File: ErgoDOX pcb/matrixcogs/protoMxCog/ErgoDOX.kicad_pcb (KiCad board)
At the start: 2 copper layers, 182.8 x 158.9 mm, 77 parts, among them J1 USB, J2 3.5mm, J3 JMP, J4 JMP, SW0:10 SW0:3, SW0:11 SW0:2, SW0:12 SW0:1, SW0:7 SW0:6, SW0:8 SW0:5, SW0:9 SW0:4, SW1:10 SW1:3, SW1:11 SW1:2, SW1:12 SW1:1, SW1:13 SW1:0, SW1:9 SW1:4, SW2:10 SW2:3, SW2:11 SW2:2, SW2:12 SW2:1, SW2:13 SW2:0, SW2:7 SW2:6, SW2:8 SW2:5, SW2:9 SW2:4, SW3:10 SW3:3, SW3:11 SW3:2, SW3:12 SW3:1, SW3:13 SW3:0, SW3:8 SW3:5, SW3:9 SW3:4, SW4:10 SW4:3, SW4:11 SW4:2, SW4:12 SW4:1, SW4:13 SW4:0, SW4:7 SW4:6, SW4:8 SW4:5, SW4:9 SW4:4, SW5:10 SW5:3, SW5:11 SW5:2, SW5:12 SW5:1, SW5:13 SW5:0, SW5:7 SW5:6, SW5:8 SW5:5, SW5:9 SW5:4, U1 TEENSY2.0, U2 MCP23018

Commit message: removing top part of PCB on switch matrix board
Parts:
- removed J2: 3.5mm, 4pin35mmAudio
- removed J3, J4: JMP, 100PITCH1X3
- removed JP1, JP2: JUMPER, GAP
- removed LED_C1: LEDc, MX_LED
- removed RA1: LEDa, RESISTOR
- removed RB1: LEDb, RESISTOR
- removed RC1: LEDc, RESISTOR
- removed STAR_1: STAR_FRONT, ErgoDOX pcb:STAR
- removed STAR_2: STAR_BACK, ErgoDOX pcb:STAR
- removed STITCHING_VIA (x11): ~, lib_footprints:STITCHING_VIA
- removed SW_RST1: SWITCH_PUSH, Buttons_Switches_SMD:SW_SPST_B3U-1000P
- removed U1: TEENSY2.0, ErgoDOX pcb:TEENSY_2.0_WITH_RESET
- removed U2: MCP23018, DIP28_300
- D1:7, D1:8: footprint DIODE -> ergodox:DIODE
- H99: footprint ErgoDOXmech -> ergodox:ErgoDOXmech
- J1: value USB -> Conn_01x18; footprint USBMINImod -> ergodox:ErgoCogs_side_con
- LED_A1, LED_B1: footprint MX_LED -> LED_SMD:LED_0805_2012Metric_Pad1.15x1.40mm_HandSolder
- R1, R2: value 2.2kΩ -> 470; footprint RESISTOR -> Resistor_SMD:R_0603_1608Metric_Pad0.98x0.95mm_HandSolder
- S1, S2: footprint STAB_PCB940 -> ergodox:STAB_PCB940
- SW0:10, SW0:11, SW0:12, SW0:7, SW0:8, SW0:9, SW1:10, SW1:11, SW1:12, SW1:13, SW1:9, SW2:10, SW2:11, SW2:12, SW2:7, SW2:8, SW2:9, SW3:10, SW3:11, SW3:12, SW3:8, SW3:9, SW4:10, SW4:11, SW4:12, SW4:7, SW4:8, SW4:9, SW5:10, SW5:11, SW5:12, SW5:7, SW5:8, SW5:9: footprint ErgoDOX pcb:MX_FLIP_DIODE -> ergodox:MX_FLIP_DIODE
- SW2:13, SW3:13, SW4:13, SW5:13: footprint ErgoDOX pcb:MX_FLIP_XX -> ergodox:MX_FLIP_DIODE
- SX0:10, SX0:11, SX1:7, SX1:8: footprint MX_FLIP -> ergodox:MX_FLIP_DIODE
- moved J1 86.5 mm to (65.0, 77.3), turned to 0 degrees
- moved LED_B1 34.2 mm to (78.7, 55.3), turned to 0 degrees
- moved R1 26.6 mm to (83.3, 55.1), turned to 0 degrees
- moved R2 19.9 mm to (87.6, 55.1), turned to 0 degrees
- moved LED_A1 9.88 mm to (73.9, 55.3)
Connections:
- J1 pad 1: Net-(J1-Pad1) -> (no net)
- J1 pad 2: Net-(J1-Pad2) -> /ROW0
- J1 pad 3: Net-(J1-Pad3) -> /ROW1
- J1 pad 4: Net-(J1-Pad4) -> /ROW2
- J1 pad 5: Net-(J1-Pad5) -> /ROW3
- J1 pad 6: GND -> /ROW4
- R1 pad 1: VCC -> /LED_B
- R1 pad 2: /SDAM -> Net-(LED_A1-Pad1)
- R2 pad 1: VCC -> /LED_A
- R2 pad 2: /SCLM -> Net-(LED_B1-Pad1)
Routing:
- net VCC: track 204.8 -> 0.57 mm, vias 2 -> 1
- net /ROW0: track 404.2 -> 274.5 mm
- net /SDAM: track 128.3 -> 0.00 mm
- net /SCLM: track 119.7 -> 0.00 mm
- net /ROW1: track 318.2 -> 210.8 mm
- net Net-(J1-Pad1): track 102.6 -> 0.00 mm
- net /ROW2: track 295.3 -> 206.6 mm
- net Net-(LED_B1-Pad1): track 119.1 -> 35.7 mm
- net /ROW3: track 238.7 -> 168.8 mm
- net Net-(LED_A1-Pad1): track 87.6 -> 22.1 mm
- net Net-(J1-Pad5): track 62.3 -> 0.00 mm
- net Net-(LED_C1-Pad1): track 127.4 -> 65.8 mm
- net /COL5: track 225.8 -> 172.7 mm
- net /ROW4: track 257.4 -> 206.2 mm
- net /COL6: track 259.5 -> 208.6 mm
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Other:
- board size 182.8 x 158.9 mm -> 182.8 x 140.1 mm
- board text removed: "5V"
- board text removed: "D+"
- board text removed: "D-"
- board text removed: "Design by Dominic Beauchamp, based on the Key64 by Nestor A. Diaz"
- board text removed: "Drawn in KiCAD by Fredrik Atmer, Bathroom Epiphanies"
- board text removed: "ErgoDox"
- board text removed: "GND"
- board text removed: "ID"
- board text removed: "Revision 01-05-2017 ProfetKeyboards"

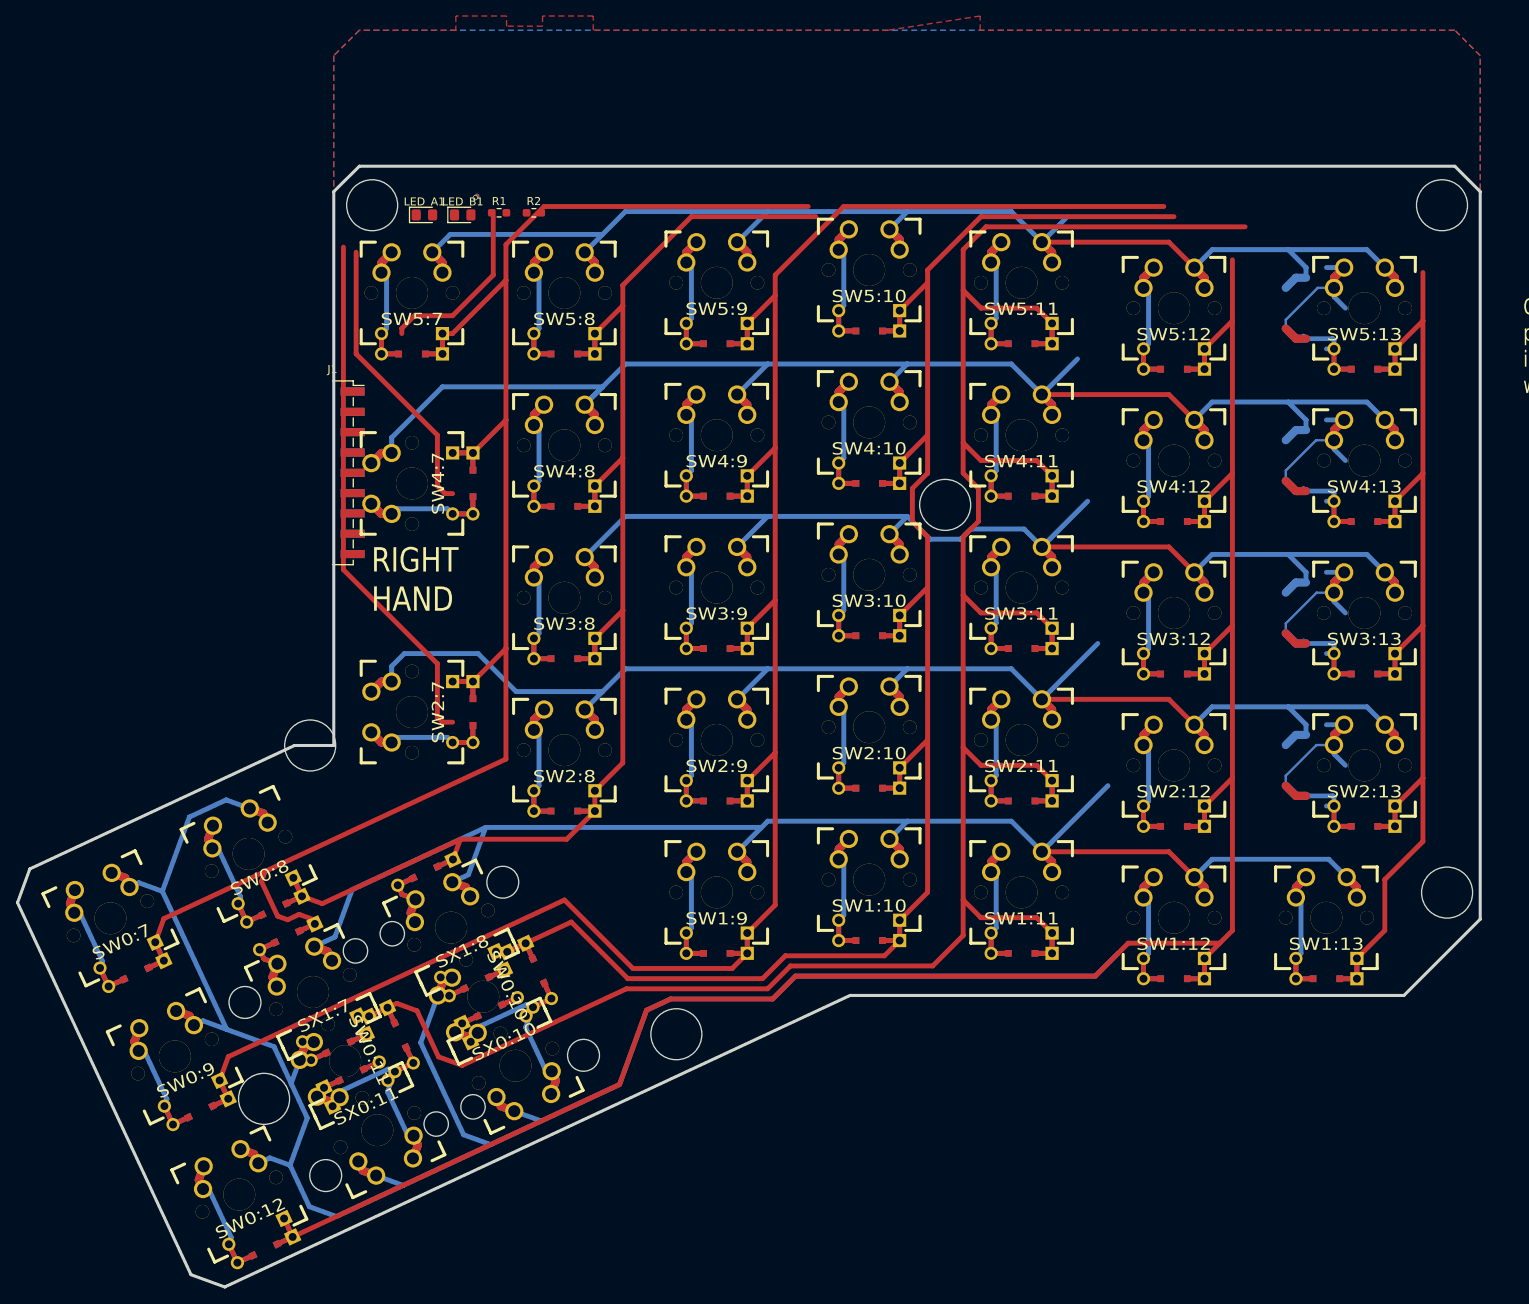
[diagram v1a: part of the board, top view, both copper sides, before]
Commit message: refactoring library structure, finishing basic matrix cog
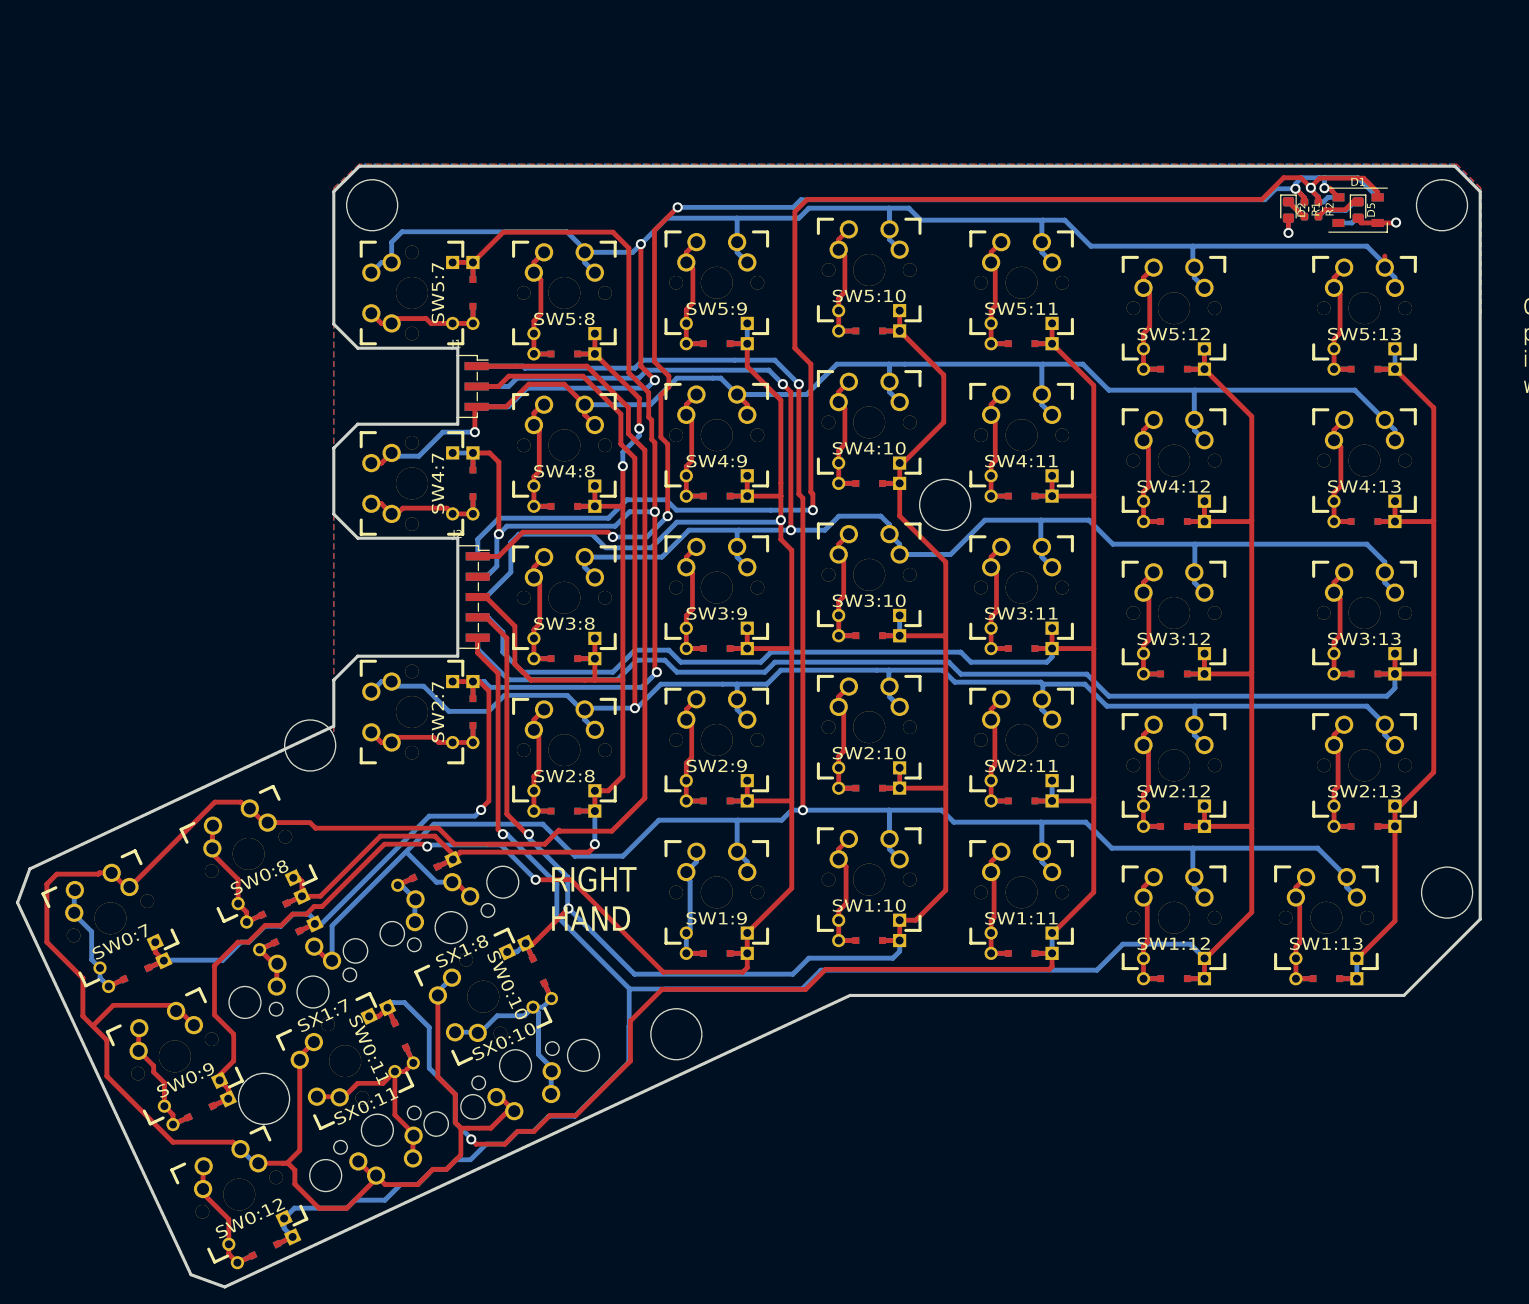
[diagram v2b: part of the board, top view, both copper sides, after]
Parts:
- removed LED_A1: LEDa, LED_SMD:LED_0805_2012Metric_Pad1.15x1.40mm_HandSolder
- added D1: WS2812B, LED_SMD:LED_WS2812B_PLCC4_5.0x5.0mm_P3.2mm, F.Cu at (190.7, 54.8)
- added D2: LED_R, LED_SMD:LED_0805_2012Metric_Pad1.15x1.40mm_HandSolder, F.Cu at (181.9, 54.7)
- added D3: LED_R, LED_SMD:LED_0805_2012Metric_Pad1.15x1.40mm_HandSolder, B.Cu at (181.9, 54.7)
- added D4: WS2812B, LED_SMD:LED_WS2812B_PLCC4_5.0x5.0mm_P3.2mm, B.Cu at (190.7, 54.8)
- added D6: LED_G, LED_SMD:LED_0805_2012Metric_Pad1.15x1.40mm_HandSolder, B.Cu at (190.7, 54.7)
- added J2: Conn_01x10, ergodox:ErgoCogs_sidecon_bot, F.Cu at (80.6, 98.0)
- added R3: 470, Resistor_SMD:R_0603_1608Metric_Pad0.98x0.95mm_HandSolder, B.Cu at (183.9, 54.6)
- added R4: 470, Resistor_SMD:R_0603_1608Metric_Pad0.98x0.95mm_HandSolder, B.Cu at (185.7, 54.6)
- D5: renamed from LED_B1; value LEDb -> LED_G
- J1: value Conn_01x18 -> Conn_01x06; footprint ergodox:ErgoCogs_side_con -> ergodox:ErgoCogs_sidecon_top
- SX0:10, SX0:11, SX1:7, SX1:8: footprint ergodox:MX_FLIP_DIODE -> ergodox:MX_FLIP
- moved D5 111.9 mm to (190.7, 54.7), turned to 270 degrees
- moved R1 100.7 mm to (183.9, 54.6), turned to 270 degrees
- moved R2 98.1 mm to (185.7, 54.6), turned to 270 degrees
- moved J1 15.8 mm to (80.5, 74.2)
- turned SW5:7 to 90 degrees
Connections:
- J1 pad 1: (no net) -> /ROW0
- J1 pad 2: /ROW0 -> /ROW1
- J1 pad 3: /ROW1 -> /ROW2
- J1 pad 4: /ROW2 -> /ROW3
- J1 pad 5: /ROW3 -> /ROW4
- J1 pad 6: /ROW4 -> /ROW5
- R1 pad 1: /LED_B -> VCC
- R2 pad 1: /LED_A -> /LED_GPIO
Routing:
- net /LED_GPIO: track 0.00 -> 169.0 mm, vias 0 -> 2
- net VCC: track 0.57 -> 166.3 mm, vias 1 -> 5
- net /COL0: track 134.3 -> 223.8 mm
- net /ROW1: track 210.8 -> 283.2 mm, vias 0 -> 2
- net Net-(LED_C1-Pad1): track 65.8 -> 0.00 mm
- net /ROW4: track 206.2 -> 168.8 mm, vias 0 -> 1
- net /ROW0: track 274.5 -> 308.4 mm
- net /COL1: track 268.8 -> 299.5 mm, vias 0 -> 1
- net Net-(D5-Pad1): track 35.7 -> 5.72 mm
- net /ROW3: track 168.8 -> 193.8 mm, vias 0 -> 2
- net Net-(SW3:13-Pad2): track 38.1 -> 13.9 mm
- net Net-(SW5:13-Pad2): track 38.0 -> 13.9 mm
- net Net-(SW4:13-Pad2): track 38.1 -> 13.9 mm
- net Net-(SW2:13-Pad2): track 37.7 -> 13.6 mm
- net /COL5: track 172.7 -> 152.2 mm, vias 0 -> 3
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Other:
- outline, holes or cut-outs redrawn
- board text removed: "FR4 Tg170° Laminate 24mil traces on 1oz copper"
- board text removed: "ProfetKeyboards.com"
